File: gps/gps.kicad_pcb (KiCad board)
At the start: 2 copper layers, 170 x 82.5 mm, 64 parts, among them J1 Conn_01x04, J2 Conn_01x04, J3 Conn_01x04, J4 Conn_01x04, J5 Conn_01x04, J6 Conn_01x04, J7 USB_B_Micro, J8 Conn_01x04, SW1 RotaryEncoder_Switch, U1 NEO-M8N, U10 M24C01-FMN, U2 TPS613226ADBV, U3 DFR0654, U4 HT16k33, U5 7seg_1x1_rgb, U6 7seg_1x1_rgb, U7 7seg_1x1_rgb, U8 CA56-12CGKWA, U9 DS3231M

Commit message: pcb update
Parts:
- moved AE1 22.1 mm to (213.0, 105.7), turned to 90 degrees
- moved C1 20.9 mm to (189.0, 89.6), turned to 180 degrees
- moved C2 20.9 mm to (185.3, 93.0), turned to 90 degrees
- moved J3 19.3 mm to (211.6, 95.3), turned to 90 degrees
- moved L1 13.8 mm to (206.8, 104.8), turned to 90 degrees
- moved C3 12.5 mm to (207.3, 101.3), turned to -90 degrees
- moved D1 8.06 mm to (209.6, 90.8), turned to 180 degrees
- moved R2 7.89 mm to (203.5, 102.2), turned to 0 degrees
- moved U1 7.60 mm to (193.3, 99.8), turned to 180 degrees
- moved R1 5.83 mm to (205.4, 90.8)
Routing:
- net GNSS_RXD: track 50.2 -> 9.18 mm
- net GNSS_TXD: track 28.1 -> 9.97 mm
- net +3V3: track 249.4 -> 262.2 mm
- net Net-(D1-A): track 4.01 -> 0.00 mm
- net GND: vias 323 -> 320

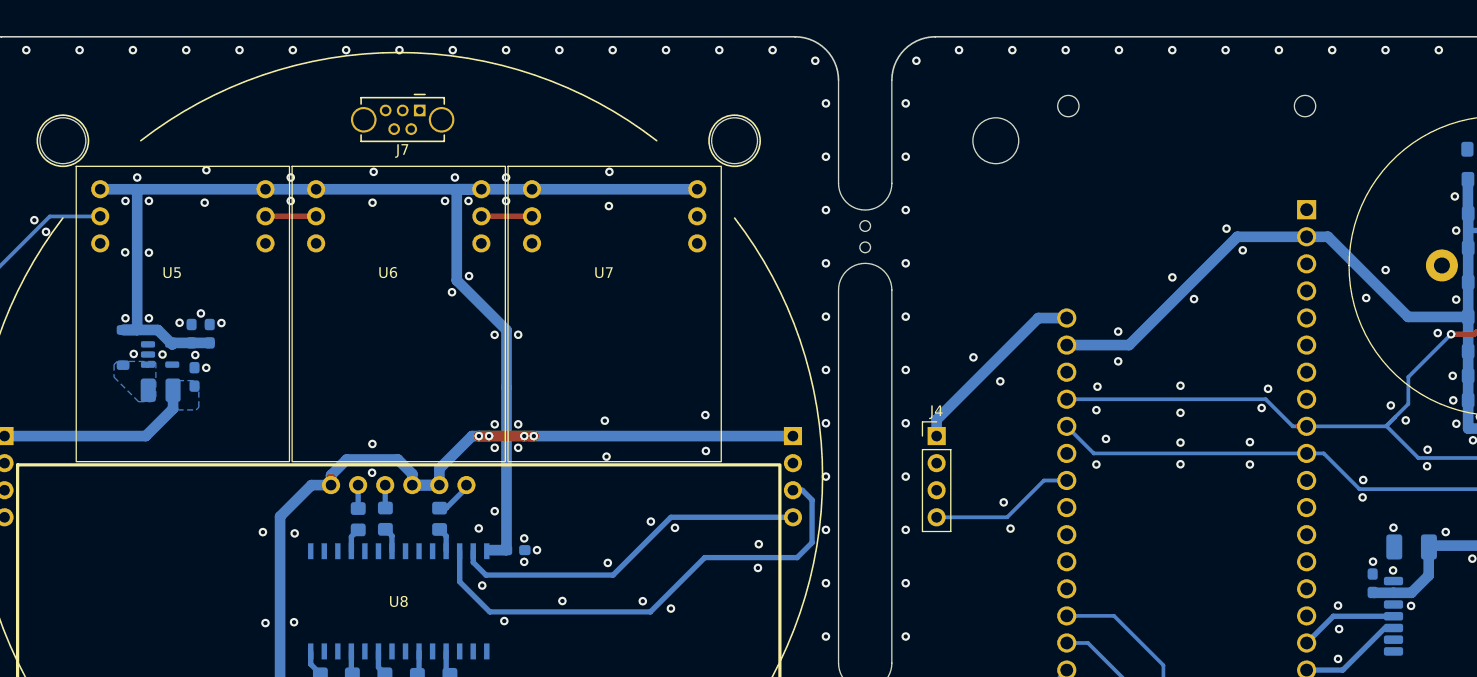
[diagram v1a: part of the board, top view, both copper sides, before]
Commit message: update pcd/sch
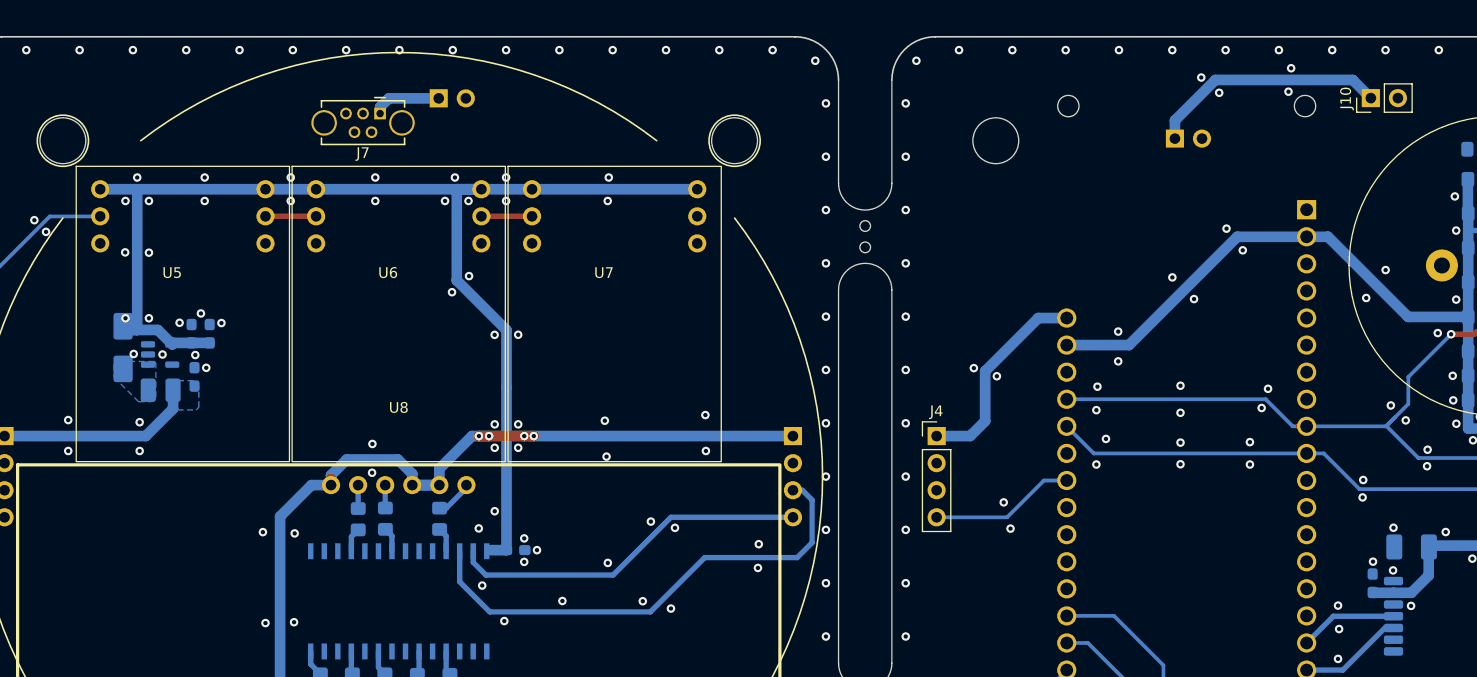
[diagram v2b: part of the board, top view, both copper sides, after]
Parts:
- added J10: Conn_01x02, Connector_PinHeader_2.54mm:PinHeader_1x02_P2.54mm_Vertical, F.Cu at (185.2, 47.5)
- added J11: Conn_01x02, Connector_PinSocket_2.54mm:PinSocket_1x02_P2.54mm_Vertical, B.Cu at (97.8, 47.5)
- added J9: Conn_01x02, Connector_PinSocket_2.54mm:PinSocket_1x02_P2.54mm_Vertical, B.Cu at (166.8, 51.3)
- D2: footprint Diode_SMD:D_SOD-123 -> Diode_SMD:D_SMA
- moved J7 3.73 mm to (92.2, 49.0)
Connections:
- J7 pad 1: +5V -> VUSB
- R14 pad 2: unconnected-(R14-Pad2) -> SQW
- U9 pad 3: unconnected-(R14-Pad2) -> SQW
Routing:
- net VUSB: track 0.00 -> 28.8 mm
- net unconnected-(R14-Pad2): track 9.33 -> 0.00 mm
- net SQW: track 0.00 -> 9.33 mm
- net VCC: track 36.3 -> 38.1 mm
- net GND: vias 320 -> 328

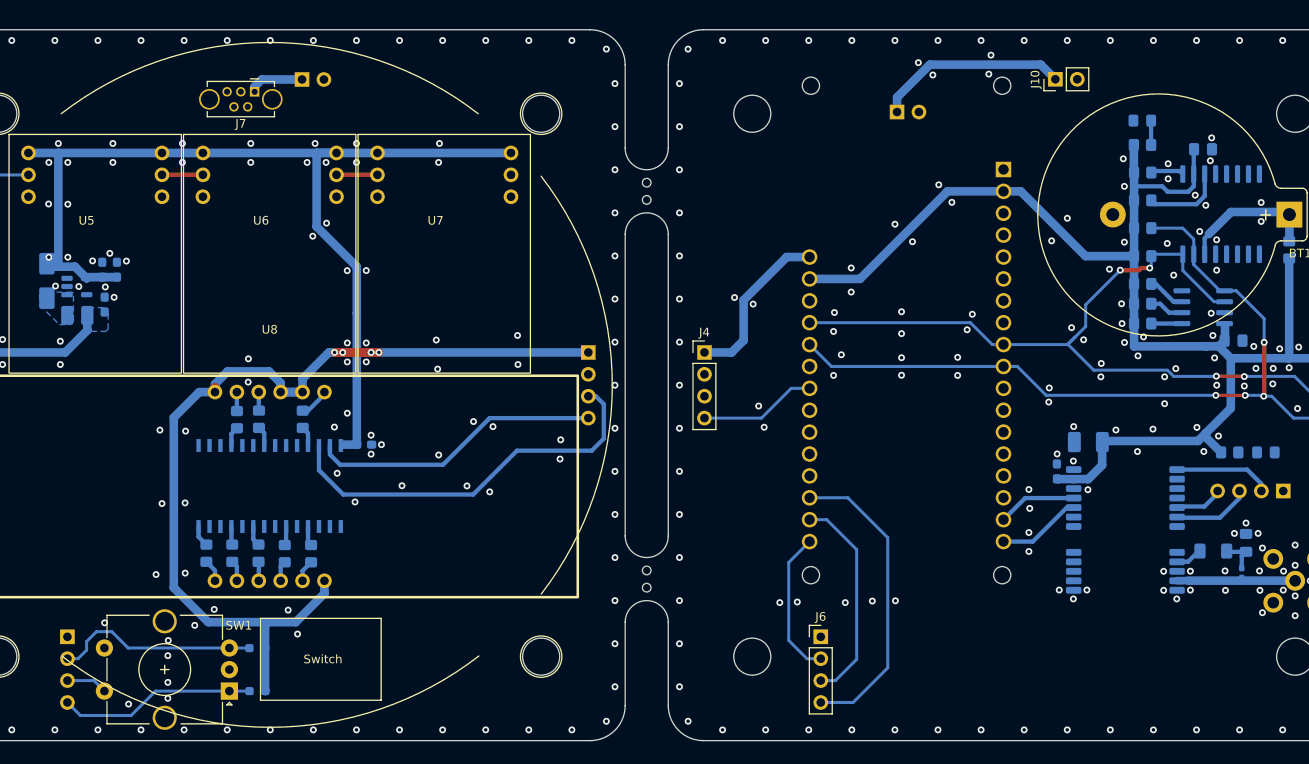
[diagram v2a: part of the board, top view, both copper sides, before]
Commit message: update pcd/sch
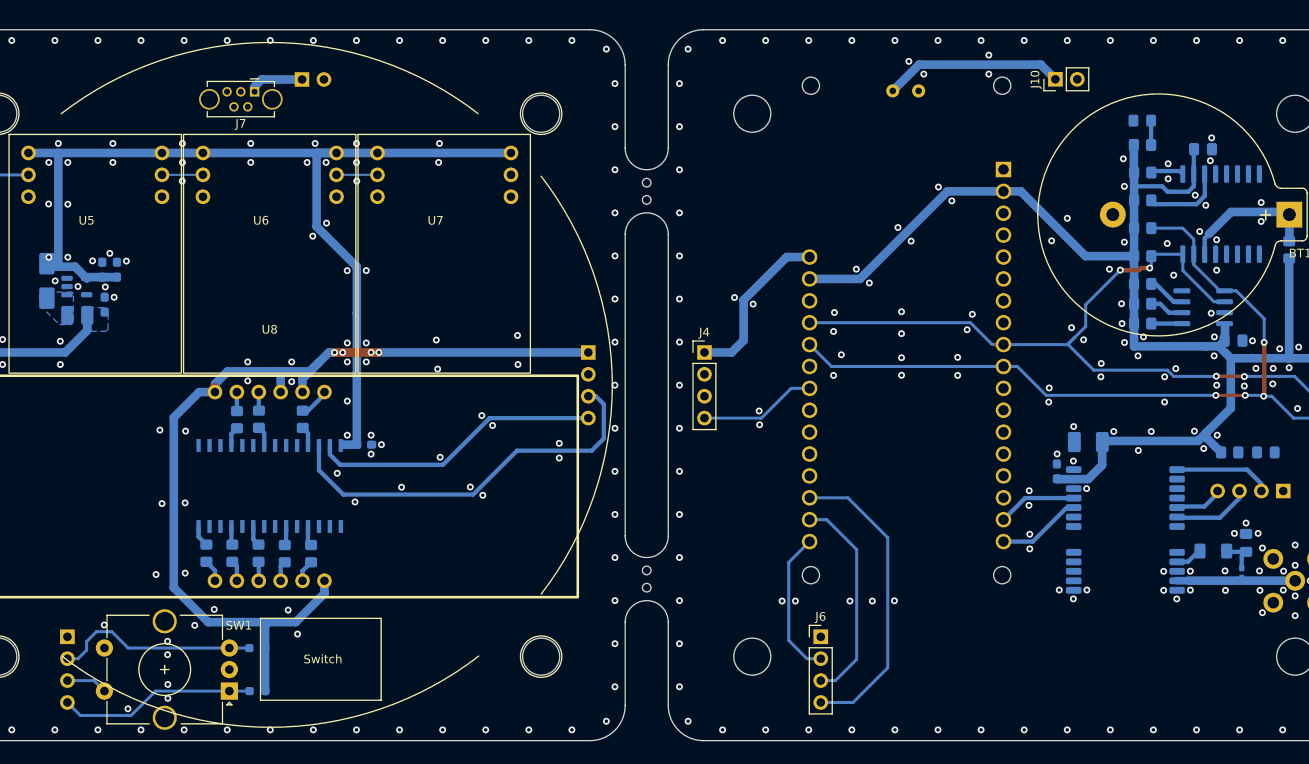
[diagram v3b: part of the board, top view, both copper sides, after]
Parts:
- removed J9: Conn_01x02, Connector_PinSocket_2.54mm:PinSocket_1x02_P2.54mm_Vertical
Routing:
- net +3V3: track 262.2 -> 264.7 mm
- net VUSB: track 28.8 -> 27.3 mm
- net GND: vias 328 -> 332

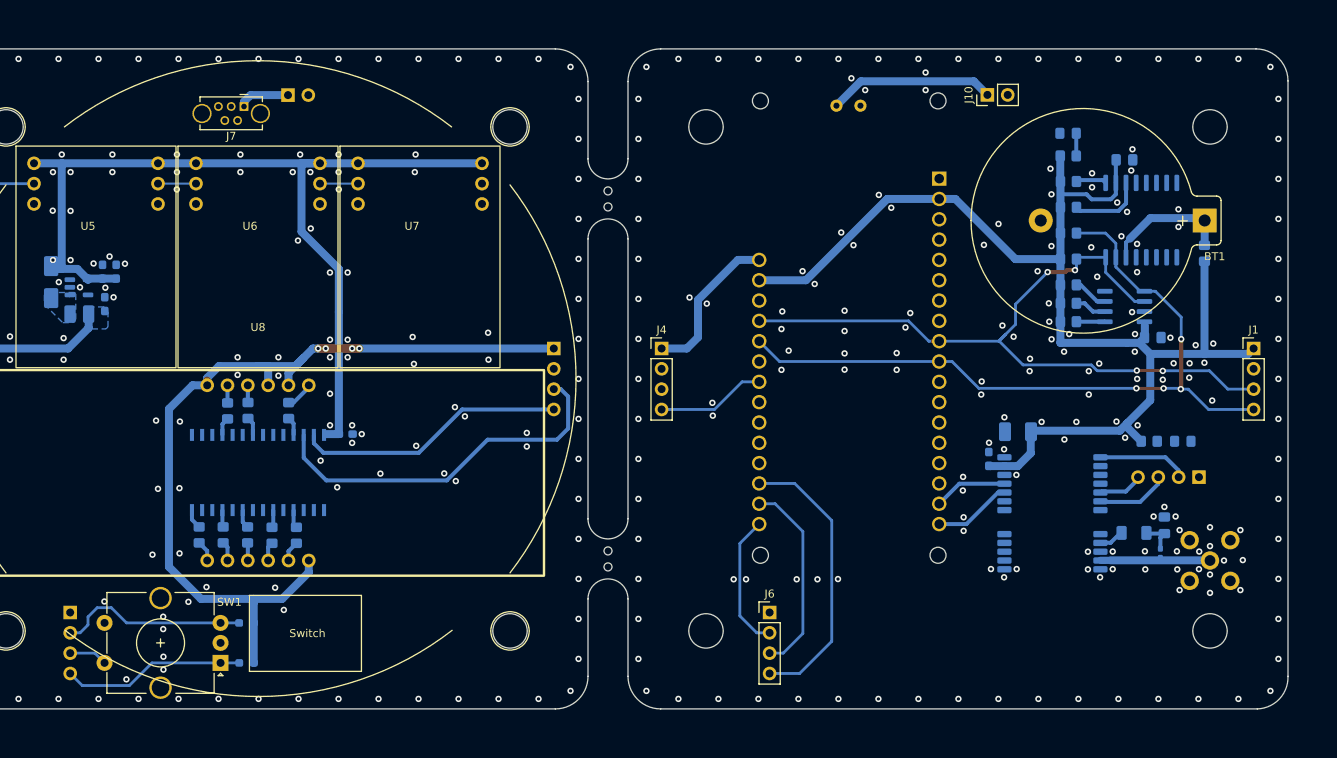
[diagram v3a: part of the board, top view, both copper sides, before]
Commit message: update pcb/housing
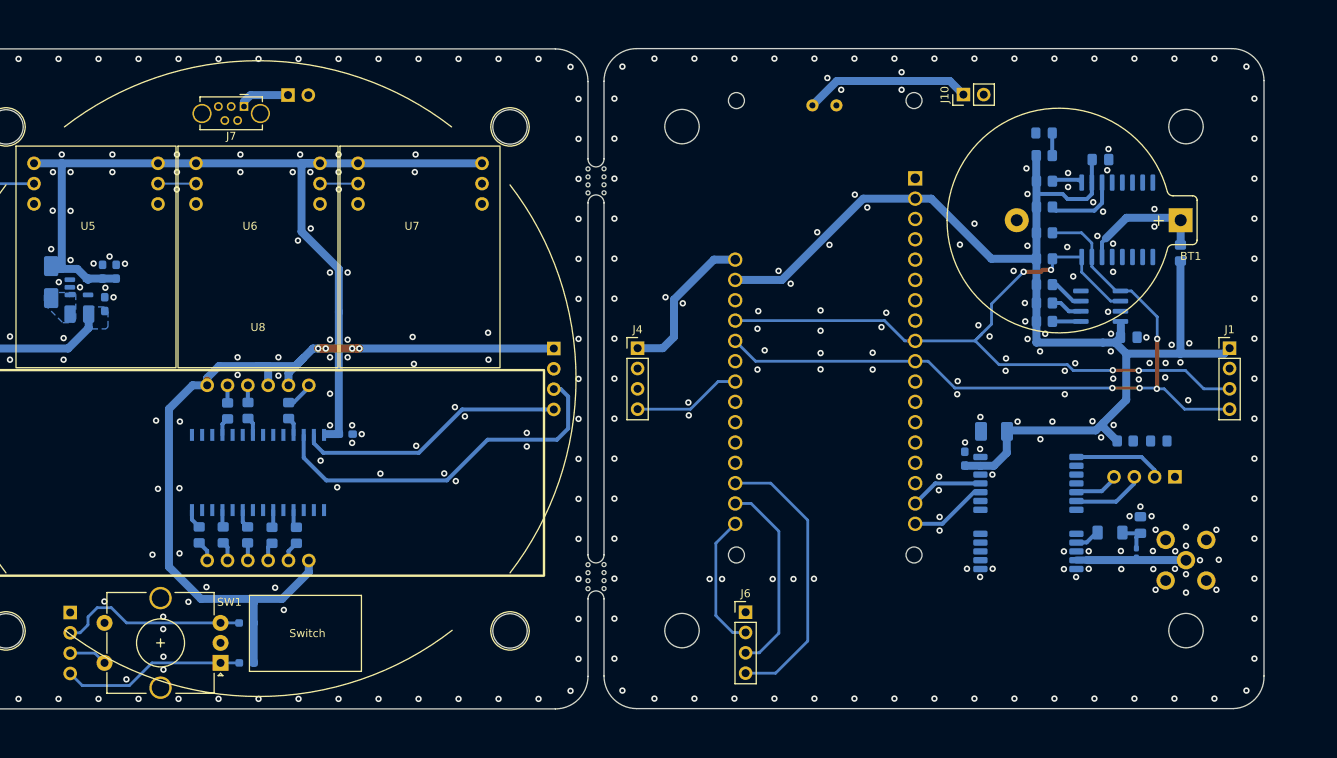
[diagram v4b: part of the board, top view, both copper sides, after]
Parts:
- moved AE1 3.00 mm to (210.0, 105.7)
- moved BT1 3.00 mm to (209.3, 63.2)
- moved C9 3.00 mm to (199.3, 55.6)
- moved J1 3.00 mm to (215.4, 79.2)
- moved J10 3.00 mm to (182.2, 47.5)
- moved J4 3.00 mm to (141.4, 79.2)
- moved J6 3.00 mm to (154.9, 112.2)
- moved R11 3.00 mm to (192.3, 64.7)
- moved R12 3.00 mm to (192.3, 68.0)
- moved R13 3.00 mm to (192.3, 58.3)
- moved R16 3.00 mm to (192.3, 55.1)
- moved REF** 3.00 mm to (210.0, 51.5)
- moved REF** 3.00 mm to (147.0, 51.5)
- moved U10 3.00 mm to (199.3, 73.9)
- moved U9 3.00 mm to (201.4, 63.1)
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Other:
- board size 170 x 82.5 mm -> 167 x 82.5 mm
- board text added: "<-- posunout nahoru"
- board text removed: "<-- otocit antena doprava"
